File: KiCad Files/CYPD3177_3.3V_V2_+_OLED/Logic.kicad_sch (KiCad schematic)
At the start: 34 parts, among them J5 0.91 OLED, J6 QWIIC, J7 Conn_01x05, J8 I2C_3.3V, Q1 DMC2990UDJ-7, SW1 GT-TC0060-H050-L1, SW2 B3U-1000P, U1 TCA9406DC, U2 INA238, U9 ATtiny3217-M

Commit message: changes
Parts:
- renumbered R5 to R10, R4 to R26, R10 to R5
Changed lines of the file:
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@@
 			"AC0AZwBlAG4AZQByAGEAdABvAHIAIABnAGUAbgBfAGkAbgBkAHUAYwB0AG8AcgAuAHAAeQAAAHdp"
 			"bmRvdyA9IHNlbGYuR2V0UGFnZSg4T3hNYxEAgEkAbgBkAHUAYwB0AG8AcgAsACAAQwBoAGEAbgBn"
-			"AGoAaQBhAG4AZwAsACAARgBYAEwAMgAyADEAMwAsACAAMgAyAA=="
+			"AGoAaQBhAG4AZwAsACAARgBYAEwAMgAyADEAMwAsACAAMgAyAJFi3l4AAJCkKY/bXgAAAAAAAAAA"
+			"AADRHlQAAAAAAKCBz47bXgAAIOtvoLlxAAAAAAAAAAAAAAAAAAAAAAAAAAAAAAAAAAAAAAAAQbcA"
+			"AEAAAAAAAAAAIAAAAAAAAAB6VpFi3l4AAPCkKY/bXgAAAAAAAAAAAABxHlQAAAAAAKCBz47bXgAA"
+			"IOtvoLlxAAAAAAAAAAAAAAAAAAAAAAAAAAAAAAAAAAAAAAAAQrcAAEAAAAAAAAAAIAAAAAAAAADa"
+			"V5Fi3l4AAFClKY/bXgAAAAAAAAAAAAARHlQAAAAAAKCBz47bXgAAIOtvoLlxAAAAAAAAAAAAAAAA"
+			"AAAAAAAAMKYpj9teAAACAAAAAAAAAEAAAAAAAAAAIAAAAAAAAAA6V5Fi3l4AALClKY/bXgAAAAAA"
+			"AAAAAACxHVQAAAAAAKCBz47bXgAAIOtvoLlxAAAAAAAAAAAAAAAAAAAAAAAAkKYpj9teAAACAAAA"
+			"AAAAAEAAAAAAAAAAIAAAAAAAAACaVJFi3l4AABCmKY/bXgAAAAAAAAAAAABRHVQAAAAAAKCBz47b"
+			"XgAAIOtvoLlxAAAAAAAAAAAAAAAAAAAAAAAA8KYpj9teAAACAAAAAAAAAEAAAAAAAAAAIAAAAAAA"
+			"AAD6VJFi3l4AAHCmKY/bXgAAAAAAAAAAAADxHFQAAAAAAKCBz47bXgAAIOtvoLlxAAAAAAAAAAAA"
+			"AAAAAAAAAAAAAAAAAAAAAAAAAAAAQ7cAAEAAAAAAAAAAIAAAAAAAAABaVJFi3l4AANCmKY/bXgAA"
+			"AAAAAAAAAACRHFQAAAAAAKCBz47bXgAAIOtvoLlxAAAAAAAAAAAAAAAAAAAAAAAAsKcpj9teAAAC"
+			"AAAAAAAAAEAAAAAAAAAAIAAAAAAAAAC6VZFi3l4AADCnKY/bXgAAAAAAAAAAAAAxHFQAAAAAAKCB"
+			"z47bXgAAIOtvoLlxAAAAAAAAAAAAAAAAAAAAAAAAAAAAAAAAAAAAAAAARLcAAEAAAAAAAAAAIAAA"
+			"AAAAAAAaVZFi3l4AAJCnKY/bXgAAAAAAAAAAAADRG1QAAAAAAKCBz47bXgAAIOtvoLlxAAAAAAAA"
+			"AAAAAAAAAAAAAAAAAAAAAAAAAAAAAAAARbcAAEAAAAAAAAAAIAAAAAAAAAB6VZFi3l4AAPCnKY/b"
+			"XgAAAAAAAAAAAABxG1QAAAAAAKCBz47bXgAAIOtvoLlxAAAAAAAAAAAAAAAAAAAAAAAAAAAAAAAA"
+			"AAAAAAAARrcAAEAAAAAAAAAAIAAAAAAAAADaWpFi3l4AAFCoKY/bXgAAAAAAAAAAAAARG1QAAAAA"
+			"AKCBz47bXgAAIOtvoLlxAAAAAAAAAAAAAAAAAAAAAAAAMKkpjw=="
 		)
 	)
@@
 		(on_board yes)
 		(dnp no)
-		(property "Reference" "R10"
+		(property "Reference" "R5"
 			(at 226.06 111.506 0)
 			(effects
@@
 			(project "CYPD3177_3.3V_V2_+_OLED"
 				(path "/a370047b-ebc6-4236-825e-9462ba7e4392/bd19bb82-a076-4c57-9538-864609224ca0"
-					(reference "R10")
+					(reference "R5")
 					(unit 1)
 				)
@@
 		(on_board yes)
 		(dnp no)
-		(property "Reference" "R5"
+		(property "Reference" "R10"
 			(at 99.568 111.76 0)
 			(effects
@@
 			(project "CYPD3177_3.3V_V2_+_OLED"
 				(path "/a370047b-ebc6-4236-825e-9462ba7e4392/bd19bb82-a076-4c57-9538-864609224ca0"
-					(reference "R5")
+					(reference "R10")
 					(unit 1)
 				)
@@
 		(on_board yes)
 		(dnp no)
-		(property "Reference" "R4"
-			(at 78.74 114.554 0)
+		(property "Reference" "R26"
+			(at 78.74 115.316 0)
 			(effects
 				(font
@@
 			(project "CYPD3177_3.3V_V2_+_OLED"
 				(path "/a370047b-ebc6-4236-825e-9462ba7e4392/bd19bb82-a076-4c57-9538-864609224ca0"
-					(reference "R4")
+					(reference "R26")
 					(unit 1)
 				)

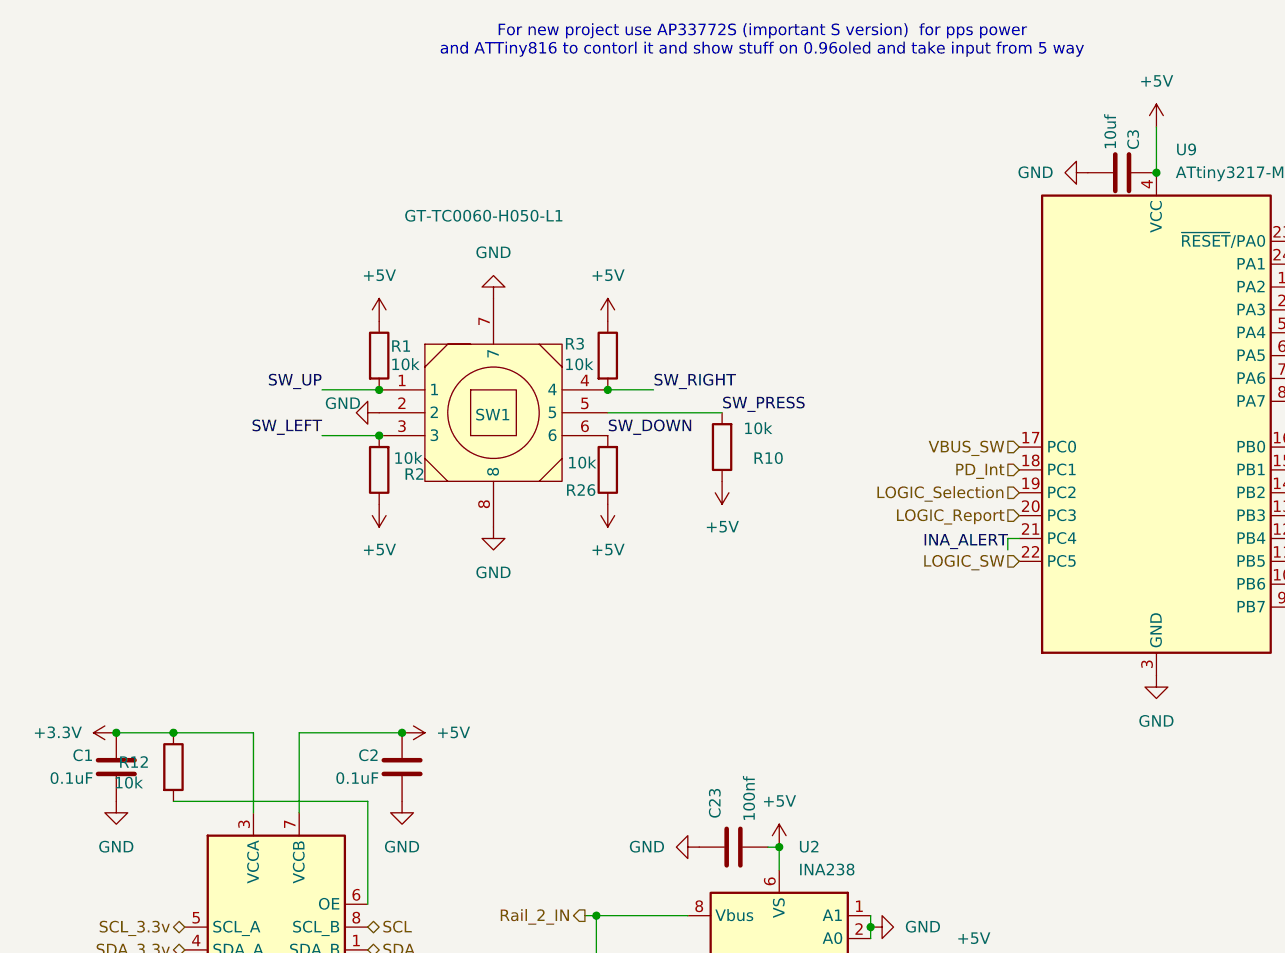
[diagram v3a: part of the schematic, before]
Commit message: finshed pcb, assigning part numbers
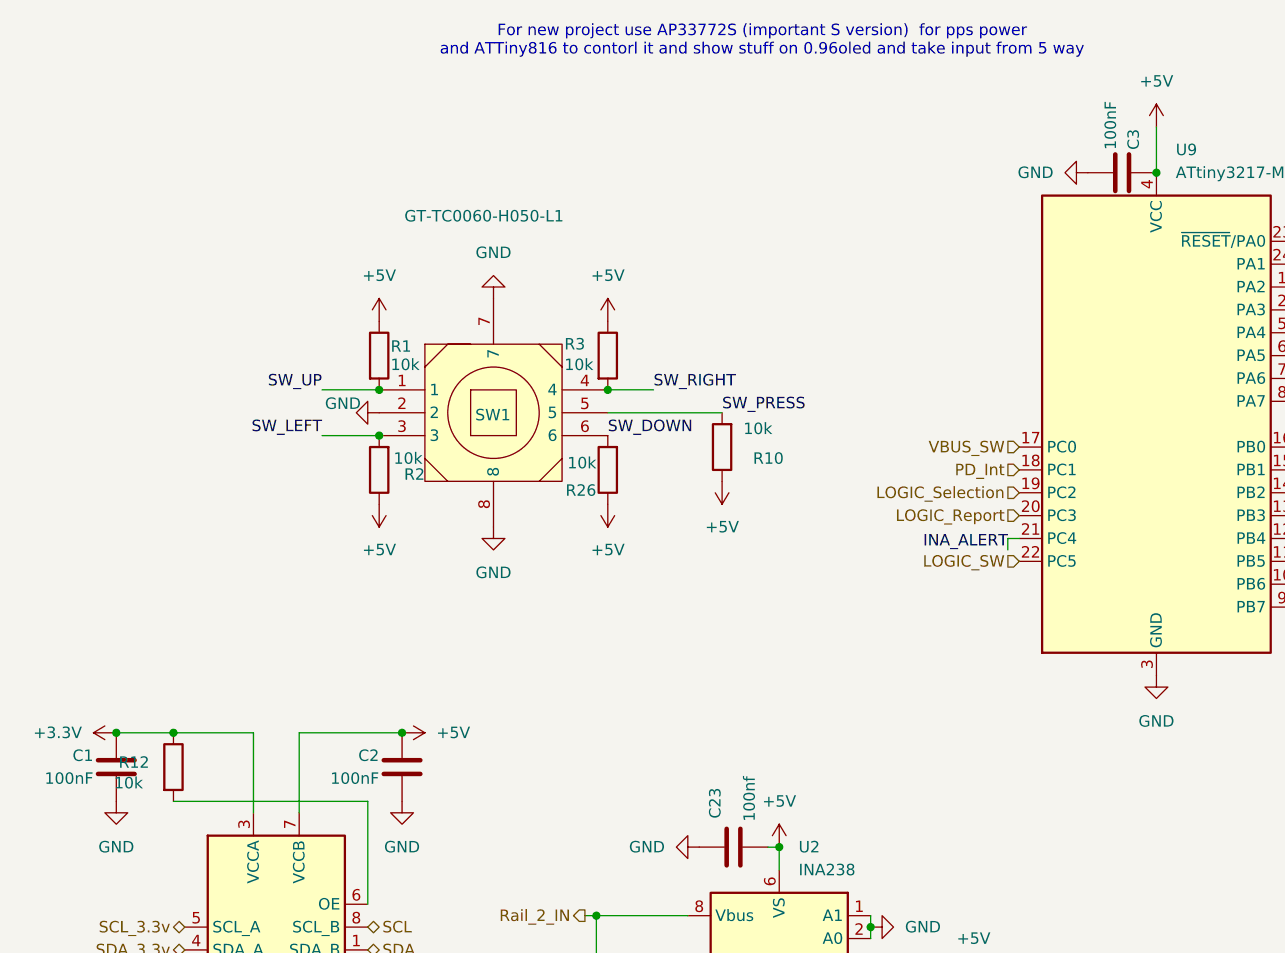
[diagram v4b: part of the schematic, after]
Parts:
- C1, C2: value 0.1uF -> 100nF
- C3: value 10uf -> 100nF
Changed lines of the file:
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@@
 			"XgAAAAAAAAAAAABxG1QAAAAAAKCBz47bXgAAIOtvoLlxAAAAAAAAAAAAAAAAAAAAAAAAAAAAAAAA"
 			"AAAAAAAARrcAAEAAAAAAAAAAIAAAAAAAAADaWpFi3l4AAFCoKY/bXgAAAAAAAAAAAAARG1QAAAAA"
-			"AKCBz47bXgAAIOtvoLlxAAAAAAAAAAAAAAAAAAAAAAAAMKkpjw=="
+			"AKCBz47bXgAAIOtvoLlxAAAAAAAAAAAAAAAAAAAAAAAAMKkpjwAAAAAAAAAAAAAAAAAAAAAAAAAA"
+			"AAAAAAAAAAAAAAAAAAAAAAAAAAAAAAAAAAAAAAAAAAAAAAAAAAAAAAAAAAAAAAAAAAAAAAAAAAAA"
+			"AAAAAAAAAAAAAAAAAAAAAAAAAAAAAAAAAAAAAAAAAAAAAAAAAAAAAAAAAAAAAAAAAAAAAAAAAAAA"
+			"AAAAAAAAAAAAAAAAAAAAAAAAAAAAAAAAAAAAAAAAAAAAAAAAAAAAAAAAAAAAAAAAAAAAAAAAAAAA"
+			"AAAAAAAAAAAAAAAAAAAAAAAAAAAAAAAAAAAAAAAAAAAAAAAAAAAAAAAAAAAAAAAAAAAAAAAAAAAA"
+			"AAAAAAAAAAAAAAAAAAAAAAAAAAAAAAAAAAAAAAAAAAAAAAAAAAAAAAAAAAAAAAAAAAAAAAAAAAAA"
+			"AAAAAAAAAAAAAAAAAAAAAAAAAAAAAAAAAAAAAAAAAAAAAAAAAAAAAAAAAAAAAAAAAAAAAAAAAAAA"
+			"AAAAAAAAAAAAAAAAAAAAAAAAAAAAAAAAAAAAAAAAAAAAAAAAAAAAAAAAAAAAAAAAAAAAAAAAAAAA"
+			"AAAAAAAAAAAAAAAAAAAAAAAAAAAAAAAAAAAAAAAAAAAAAAAAAAAAAAAAAAAAAAAAAAAAAAAAAAAA"
+			"AAAAAAAAAAAAAAAAAAAAAAAAAAAAAAAAAAAAAAAAAAAAAAAAAAAAAAAAAAAAAAAAAAAAAAAAAAAA"
+			"AAAAAAAAAAAAAAAAAAAAAAAAAAAAAAAAAAAAAAAAAAAAAAAAAAAAAAAAAAAAAAAAAAAAAAAAAAAA"
+			"AAAAAAAAAAAAAAAAAAAAAAAAAAAAAAAAAAAAAAAAAAAAAAAAAAAAAAAAAAAAAAAAAAAAAAAAAAAA"
+			"AAAAAAAAAAAAAAAAAAAAAAAAAAAAAAAAAAAAAAAAAAAAAAAAAAAAAAAAAAAAAAAAAAAAAAAAAAAA"
+			"AAAAAAAAAAAAAAAAAAAAAAAAAAAAAAAAAAAAAAAAAAAAAAAAAAAAAAAAAAAAAAAAAAAAAAAAAAAA"
+			"AAAAAAAAAAAAAAAAAAAAAAAAAAAAAAAAAAAAAAAAAAAAAAAAAAAAAAAAAAAAAAAAAAAAAAAAAAAA"
+			"AAAAAAAAAAAAAAAAAAAAAAAAAAAAAAAAAAAAAAAAAAAAAAAAAAAAAAAAAAAAAAAAAAAAAAAAAAAA"
+			"AAAAAAAAAAAAAAAAAAAAAAAAAAAAAAAAAAAAAAAAAAAAAAAAAAAAAAAAAAAAAAAAAAAAAAAAAAAA"
+			"AAAAAAAAAAAAAAAAAAAAAAAAAAAAAAAAAAAAAAAAAAAAAAAAAAAAAAAAAAAAAAAAAAAAAAAAAAAA"
+			"AAAAAAAAAAAAAAAAAAAAAAAAAAAAAAAAAAAAAAAAAAAAAAAAAA=="
 		)
 	)
@@
 			)
 		)
-		(property "Value" "0.1uF"
+		(property "Value" "100nF"
 			(at 22.86 147.32 0)
 			(effects
@@
 			)
 		)
-		(property "Value" "10uf"
+		(property "Value" "100nF"
 			(at 135.89 77.47 0)
 			(effects
@@
 			)
 		)
-		(property "Value" "0.1uF"
+		(property "Value" "100nF"
 			(at 54.61 147.32 0)
 			(effects

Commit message: changes
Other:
- note removed: "For new project use AP33772S (important S version) for pps power and ATTiny816 to contorl it and show stuff on 0.96oled and take input from 5 way"
- title: (none) -> USB PD PPS for breadboards

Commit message: almost finished
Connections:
- net +5V: now also C23.1; no longer C23.2
- net GND: now also C23.2; no longer C23.1
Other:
- note added: "5 way switch for user input"
- note added: "80% of the GPIO are conected just for status of IC and are opend drain or smth, not so important."
- note added: "Dedicated Current & Voltage reader for Rail_2 line"
- note added: "I2C pull ups optional, just as backup."
- note added: "MCU for settings Voltage&Current and reading inputs of user"
- note added: "Mosfet to enable/disbale LED, to tell users Status of PCB"
- note added: "Pin headers & connectors"
- note added: "Reset Button for Attiny"
- note added: "Shifts 3.3v I2C to 5V (also has built in pull ups)"
- moved on the sheet: C23, C3, D6, J5, J6, J7, J8, R1, R10, R13, R2, R26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

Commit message: now final version, changed routing completly and should be better board
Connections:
- net INA_ALERT: now also U9.2 (PA3); no longer U9.21 (PC4)
- net LOGIC_Report: now also U9.21 (PC4); no longer U9.20 (PC3)
- net LOGIC_SW: now also U9.8 (PA7); no longer U9.22 (PC5)
- net LOGIC_Selection: now also U9.20 (PC3); no longer U9.19 (PC2)
- net PGOOD: now also U9.11 (PB5); no longer U9.7 (PA6)
- net PGOOD_Logic: now also U9.24 (PA1); no longer U9.10 (PB6)
- net SW_LEFT: now also U9.19 (PC2); no longer U9.1 (PA2)
- net SW_PRESS: now also U9.10 (PB6); no longer U9.8 (PA7)
- net SW_RIGHT: now also U9.1 (PA2); no longer U9.2 (PA3)
- net SW_UP: now also U9.22 (PC5); no longer U9.24 (PA1)
- net VBUS_Fault: now also U9.7 (PA6); no longer U9.11 (PB5)
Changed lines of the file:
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@@
+	(wire
+		(pts
+			(xy 81.28 92.71) (xy 81.28 91.44)
+		)
+		(stroke
+			(width 0)
+			(type default)
+		)
+	)
 	(wire
 		(pts
@@
 	(wire
 		(pts
+			(xy 81.28 64.77) (xy 81.28 63.5)
+		)
+		(stroke
+			(width 0)
+			(type default)
+		)
+	)
+	(wire
+		(pts
 			(xy 25.4 142.24) (xy 31.75 142.24)
 		)
@@
 	(wire
 		(pts
+			(xy 81.28 59.69) (xy 81.28 58.42)
+		)
+		(stroke
+			(width 0)
+			(type default)
+		)
+	)
+	(wire
+		(pts
+			(xy 81.28 62.23) (xy 81.28 60.96)
+		)
+		(stroke
+			(width 0)
+			(type default)
+		)
+	)
+	(wire
+		(pts
 			(xy 66.04 38.1) (xy 66.04 43.18)
 		)
@@
 	(wire
 		(pts
+			(xy 50.8 80.01) (xy 50.8 78.74)
+		)
+		(stroke
+			(width 0)
+			(type default)
+		)
+	)
+	(wire
+		(pts
 			(xy 31.75 149.86) (xy 53.34 149.86)
 		)
@@
 	(wire
 		(pts
+			(xy 81.28 90.17) (xy 81.28 88.9)
+		)
+		(stroke
+			(width 0)
+			(type default)
+		)
+	)
+	(wire
+		(pts
 			(xy 100.33 147.32) (xy 100.33 153.67)
 		)
@@
 	(wire
 		(pts
-			(xy 91.44 58.42) (xy 81.28 58.42)
-		)
-		(stroke
-			(width 0)
-			(type default)
-		)
-	)
-	(wire
-		(pts
 			(xy 120.65 139.7) (xy 120.65 142.24)
 		)
@@
 	(wire
 		(pts
-			(xy 81.28 69.85) (xy 81.28 68.58)
-		)
-		(stroke
-			(width 0)
-			(type default)
-		)
-	)
-	(wire
-		(pts
 			(xy 200.66 101.6) (xy 204.47 101.6)
 		)
@@
 	(wire
 		(pts
+			(xy 50.8 87.63) (xy 50.8 86.36)
+		)
+		(stroke
+			(width 0)
+			(type default)
+		)
+	)
+	(wire
+		(pts
 			(xy 100.33 147.32) (xy 110.49 147.32)
 		)
@@
 	(wire
 		(pts
-			(xy 49.53 85.09) (xy 49.53 83.82)
-		)
-		(stroke
-			(width 0)
-			(type default)
-		)
-	)
-	(wire
-		(pts
 			(xy 130.81 162.56) (xy 142.24 162.56)
 		)
@@
 	(wire
 		(pts
-			(xy 81.28 54.61) (xy 81.28 53.34)
-		)
-		(stroke
-			(width 0)
-			(type default)
-		)
-	)
-	(wire
-		(pts
-			(xy 49.53 83.82) (xy 50.8 83.82)
-		)
-		(stroke
-			(width 0)
-			(type default)
-		)
-	)
-	(wire
-		(pts
 			(xy 104.14 161.29) (xy 110.49 161.29)
 		)
@@
 	(wire
 		(pts
-			(xy 81.28 92.71) (xy 81.28 91.44)
-		)
-		(stroke
-			(width 0)
-			(type default)
-		)
-	)
-	(wire
-		(pts
 			(xy 104.14 161.29) (xy 104.14 163.83)
 		)
@@
 	)
 	(label "PowerLED_EN"
-		(at 81.28 60.96 0)
+		(at 81.28 62.23 0)
 		(effects
 			(font
@@
 	)
 	(label "SW_PRESS"
-		(at 81.28 69.85 0)
+		(at 81.28 90.17 0)
 		(effects
 			(font
@@
 	)
 	(label "Failer_EN"
-		(at 81.28 63.5 0)
+		(at 81.28 64.77 0)
 		(effects
 			(font
@@
 	)
 	(label "SW_UP"
-		(at 81.28 54.61 0)
-		(effects
-			(font
-				(size 1.27 1.27)
-			)
-			(justify left bottom)
+		(at 50.8 87.63 180)
+		(effects
+			(font
+				(size 1.27 1.27)
+			)
+			(justify right bottom)
 		)
 	)
@@
 		)
 	)
-	(label "SW_RIGHT"
-		(at 91.44 58.42 0)
-		(effects
-			(font
-				(size 1.27 1.27)
-			)
-			(justify left bottom)
-		)
-	)
 	(label "INA_ALERT"
-		(at 49.53 85.09 180)
-		(effects
-			(font
-				(size 1.27 1.27)
-			)
-			(justify right bottom)
+		(at 81.28 59.69 0)
+		(effects
+			(font
+				(size 1.27 1.27)
+			)
+			(justify left bottom)
 		)
 	)
@@
 		)
 	)
+	(label "SW_RIGHT"
+		(at 81.28 57.15 0)
+		(effects
+			(font
+				(size 1.27 1.27)
+			)
+			(justify left bottom)
+		)
+	)
 	(label "SW_LEFT"
-		(at 81.28 57.15 0)
-		(effects
-			(font
-				(size 1.27 1.27)
-			)
-			(justify left bottom)
+		(at 50.8 80.01 180)
+		(effects
+			(font
+				(size 1.27 1.27)
+			)
+			(justify right bottom)
 		)
 	)
 	(hierarchical_label "LOGIC_Selection"
 		(shape input)
-		(at 50.8 78.74 180)
+		(at 50.8 81.28 180)
 		(effects
 			(font
@@
 	(hierarchical_label "LOGIC_SW"
 		(shape input)
-		(at 50.8 86.36 180)
-		(effects
-			(font
-				(size 1.27 1.27)
-			)
-			(justify right)
+		(at 81.28 68.58 0)
+		(effects
+			(font
+				(size 1.27 1.27)
+			)
+			(justify left)
 		)
 	)
@@
 	(hierarchical_label "PGOOD_Logic"
 		(shape output)
-		(at 81.28 88.9 0)
+		(at 81.28 53.34 0)
 		(effects
 			(font
@@
 	(hierarchical_label "PGOOD"
 		(shape output)
-		(at 81.28 66.04 0)
+		(at 81.28 86.36 0)
 		(effects
 			(font
@@
 	(hierarchical_label "LOGIC_Report"
 		(shape input)
-		(at 50.8 81.28 180)
+		(at 50.8 83.82 180)
 		(effects
 			(font
@@
 	(hierarchical_label "VBUS_Fault"
 		(shape output)
-		(at 81.28 86.36 0)
-		(effects
-			(font
+		(at 81.28 66.04 0)
+		(effects
+			(font

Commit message: changes
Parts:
- U2: value INA238 -> INA237
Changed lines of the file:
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@@
 			)
 		)
-		(property "Value" "INA238"
+		(property "Value" "INA237"
 			(at 116.84 151.892 0)
 			(effects
